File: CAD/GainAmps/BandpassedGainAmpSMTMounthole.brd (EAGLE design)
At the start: 9 parts, among them IC2 OPA202IDGKR

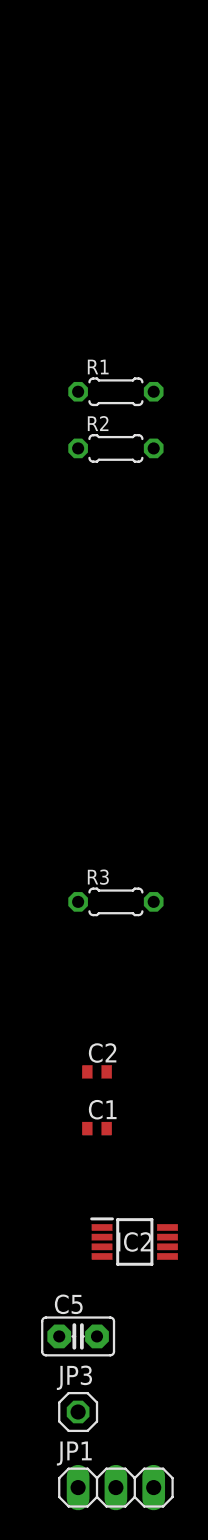
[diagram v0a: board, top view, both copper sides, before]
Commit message: moved, added production files for gain amps
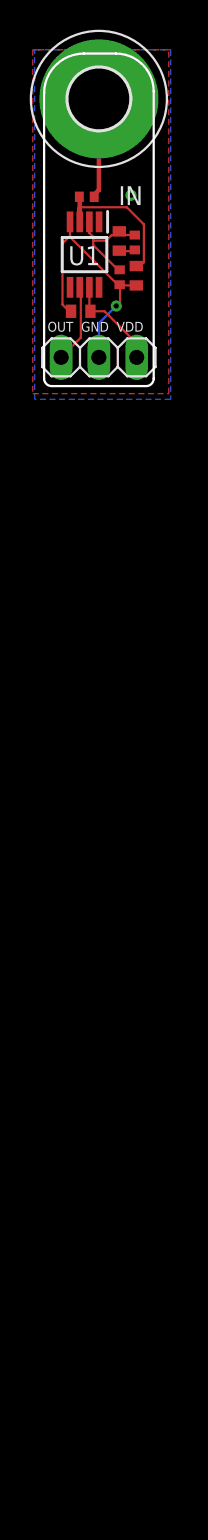
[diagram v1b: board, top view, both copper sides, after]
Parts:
- removed C5: (no value), capacitor-wima:C2.5-2
- removed IC2: OPA202IDGKR, OPA202IDGKR:SOP65P490X110-8N
- removed JP3: (no value), pinhead:1X01
- added C3: (no value), rcl:C0402
- added H1: MOUNT-PAD-ROUND4.1, holes:4,1-PAD
- added U1: OPA202IDGKR, OPA202IDGKR:SOP65P490X110-8N
- R1, R2, R3: device rcl:0204/5 -> rcl:R0402
- moved JP1 76.0 mm to (5.21, 3.58), turned to 180 degrees
- moved C1 57.4 mm to (7.72, 9.07), turned to 90 degrees
- moved C2 55.9 mm to (6.58, 11.4), turned to 270 degrees
- moved R3 47.4 mm to (4.39, 14.4), turned to 180 degrees
- moved R2 13.9 mm to (7.62, 11.3), turned to 270 degrees
- moved R1 7.70 mm to (6.60, 8.97), turned to 90 degrees
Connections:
- removed net OUTA: JP1.3
- net +IN: now also C1.2, U1.3; no longer C2.2, IC2.3
- net -IN: now also C2.1, U1.2; no longer C1.1, IC2.2
- net GND: now also C1.1, C3.1, U1.4; no longer C2.1, C5.1, IC2.4
- net IN: now also H1.B4,1; no longer JP3.1
- net N$3: now also C2.2; no longer C1.2
- net OUT: now also JP1.3, U1.6; no longer IC2.6
- net VDD: now also C3.2, U1.7; no longer C5.2, IC2.7
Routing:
- net GND: track 0.00 -> 18.0 mm, vias 0 -> 2
- net +IN: track 0.00 -> 11.6 mm
- net -IN: track 0.00 -> 7.88 mm
- net IN: track 0.00 -> 6.71 mm
- net VDD: track 0.00 -> 6.58 mm
- net OUT: track 0.00 -> 5.29 mm
- net N$3: track 0.00 -> 1.34 mm
- added copper zone on layer 1, net GND
- added copper zone on layer 16, net GND
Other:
- board outline added: 7.4 x 22.4 mm
- board text added: "IN"
- board text added: "OUT GND VDD"

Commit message: fixed edge plating
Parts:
- moved R1 0.25 mm to (6.35, 8.97)
- moved R2 0.25 mm to (7.37, 11.3)
- moved C1 0.25 mm to (7.47, 9.07)
- moved C2 0.25 mm to (6.32, 11.4)
- moved U1 0.25 mm to (3.99, 10.5)
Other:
- board size 7.4 x 22.4 mm -> 7.4 x 21.5 mm

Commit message: fixes
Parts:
- removed R3: 1K, rcl:R0402
- added REF: (no value), pinhead:1X01
- moved R1 5.51 mm to (5.89, 14.5), turned to 0 degrees
- moved C1 3.62 mm to (6.38, 12.5), turned to 270 degrees
- moved C2 1.91 mm to (7.47, 9.88)
- moved R2 1.63 mm to (6.35, 10.0)
- moved C3 0.38 mm to (3.61, 6.68)
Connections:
- removed net +IN: C1.2, R3.2, U1.3
- removed net N$3: C2.2, R2.2
- new net +REF: REF.1, U1.3
- new net R1C1: C1.1, R1.2
- net -IN: now also C1.2; no longer R1.2
- net GND: now also JP1.3; no longer C1.1, JP1.2, R1.1
- net IN: now also R1.1; no longer R3.1
- net OUT: now also C2.2, JP1.1, R2.2; no longer JP1.3
- net VDD: now also JP1.2; no longer JP1.1
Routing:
- net +IN: track 11.7 -> 0.00 mm
- net GND: track 18.0 -> 9.83 mm, vias 2 -> 0
- net OUT: track 5.39 -> 10.6 mm
- net +REF: track 0.00 -> 2.36 mm
- net -IN: track 7.88 -> 5.72 mm
- net VDD: track 6.69 -> 5.13 mm
- net N$3: track 1.34 -> 0.00 mm
- net R1C1: track 0.00 -> 1.29 mm
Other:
- outline, holes or cut-outs redrawn
- board text added: "GND VDD OUT"
- board text removed: "OUT GND VDD"
